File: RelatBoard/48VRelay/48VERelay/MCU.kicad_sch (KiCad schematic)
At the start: 40 parts, among them U1 ESP32-WROOM-32UE, U3 W5500, Y2 ABM3C-25.000MHZ-D4Y-T

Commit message: Update tx / rx nets
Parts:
- R18, R20: footprint Resistor_SMD:R_0603_1608Metric -> Resistor_SMD:R_0201_0603Metric
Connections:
- net PHY_R_RXN: now reaches R16.1, U3.5 (RXN)
- net PHY_RC_RXN: now reaches C17.1, R16.2, R21.1
- net PHY_RC_RXP: now reaches C19.1, R17.2, R22.1
- net PHY_R_TXN: now reaches R7.1, U3.1 (TXN)
- net PHY_R_TXP: now reaches R8.1, U3.2 (TXP)
- net PHY_R_RXP: now reaches R17.1, U3.6 (RXP)
- net TX_N renamed PHY_RC_TXN
- net TX_P renamed PHY_RC_TXP
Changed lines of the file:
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@@
 		)
 	)
+	(label "PHY_R_RXP"
+		(at 210.82 106.68 270)
+		(effects
+			(font
+				(size 1.27 1.27)
+			)
+			(justify right bottom)
+		)
+	)
 	(label "LINK_LED"
 		(at 212.09 129.54 0)
@@
 		)
 	)
+	(label "PHY_RC_TXP"
+		(at 224.79 99.06 90)
+		(effects
+			(font
+				(size 1.27 1.27)
+			)
+			(justify left bottom)
+		)
+	)
 	(label "RX_N"
 		(at 251.46 104.14 0)
@@
 		)
 	)
+	(label "PHY_R_TXP"
+		(at 210.82 99.06 90)
+		(effects
+			(font
+				(size 1.27 1.27)
+			)
+			(justify left bottom)
+		)
+	)
+	(label "PHY_RC_RXN"
+		(at 223.52 104.14 270)
+		(effects
+			(font
+				(size 1.27 1.27)
+			)
+			(justify right bottom)
+		)
+	)
 	(label "Ether_CS"
 		(at 161.29 96.52 0)
@@
 		)
 	)
+	(label "PHY_R_RXN"
+		(at 208.28 104.14 270)
+		(effects
+			(font
+				(size 1.27 1.27)
+			)
+			(justify right bottom)
+		)
+	)
 	(label "PHY_VDD"
 		(at 167.64 83.82 0)
@@
 		)
 	)
+	(label "PHY_R_TXN"
+		(at 208.28 96.52 90)
+		(effects
+			(font
+				(size 1.27 1.27)
+			)
+			(justify left bottom)
+		)
+	)
 	(label "JTAG_TMS"
 		(at 115.57 71.12 0)
@@
 		)
 	)
+	(label "PHY_RC_RXP"
+		(at 224.79 106.68 270)
+		(effects
+			(font
+				(size 1.27 1.27)
+			)
+			(justify right bottom)
+		)
+	)
 	(label "Ether_MOSI"
 		(at 161.29 104.14 0)
@@
 		)
 	)
+	(label "PHY_RC_TXN"
+		(at 222.2454 96.52 90)
+		(effects
+			(font
+				(size 1.27 1.27)
+			)
+			(justify left bottom)
+		)
+	)
 	(label "RX_P"
 		(at 251.46 106.68 0)
@@
 			)
 		)
-		(property "Footprint" "Resistor_SMD:R_0603_1608Metric"
+		(property "Footprint" "Resistor_SMD:R_0201_0603Metric"
 			(at 238.76 90.17 0)
 			(hide yes)
@@
 			)
 		)
-		(property "Footprint" "Resistor_SMD:R_0603_1608Metric"
+		(property "Footprint" "Resistor_SMD:R_0201_0603Metric"
 			(at 228.6 90.17 0)
 			(hide yes)

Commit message: update tx/rx eth routing
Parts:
- R21, R22: footprint Resistor_SMD:R_0201_0603Metric -> Resistor_SMD:R_01005_0402Metric
- R26: footprint (none) -> Resistor_SMD:R_0402_1005Metric
- R6: footprint Resistor_SMD:R_0603_1608Metric -> Resistor_SMD:R_0402_1005Metric
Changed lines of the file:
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@@
 			)
 		)
-		(property "Footprint" "Resistor_SMD:R_0201_0603Metric"
+		(property "Footprint" "Resistor_SMD:R_01005_0402Metric"
 			(at 234.95 111.76 0)
 			(hide yes)
@@
 			)
 		)
-		(property "Footprint" "Resistor_SMD:R_0201_0603Metric"
+		(property "Footprint" "Resistor_SMD:R_01005_0402Metric"
 			(at 228.6 110.49 0)
 			(hide yes)
@@
 			)
 		)
-		(property "Footprint" "Resistor_SMD:R_0603_1608Metric"
+		(property "Footprint" "Resistor_SMD:R_0402_1005Metric"
 			(at 227.33 142.24 0)
 			(hide yes)
@@
 			)
 		)
-		(property "Footprint" ""
+		(property "Footprint" "Resistor_SMD:R_0402_1005Metric"
 			(at 60.452 46.99 90)
 			(hide yes)

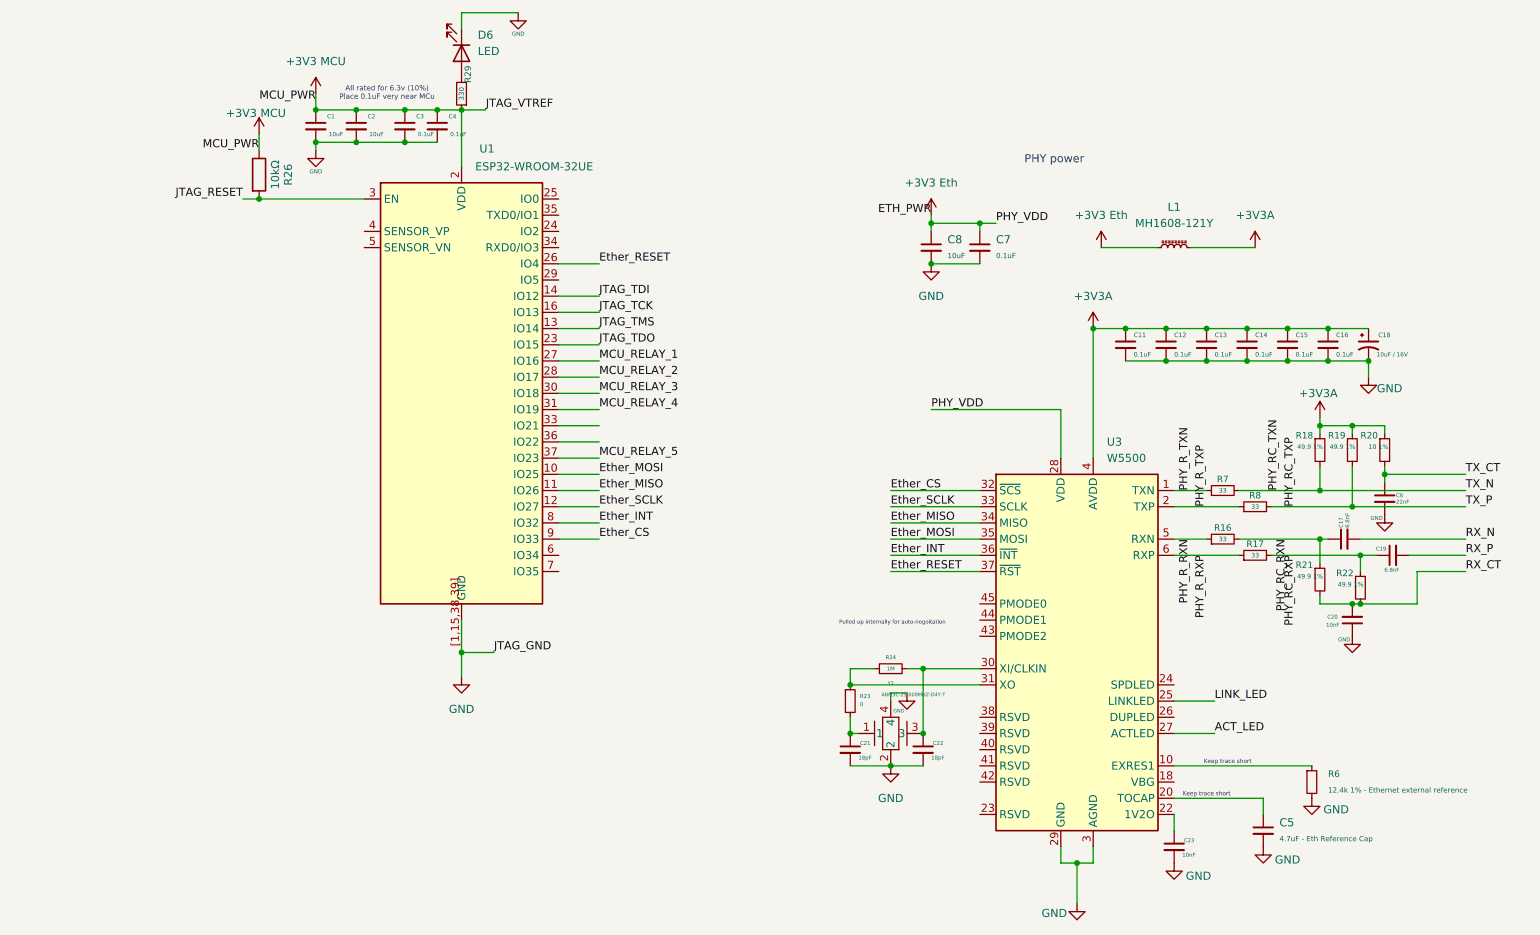
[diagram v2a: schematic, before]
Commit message: JTAG left
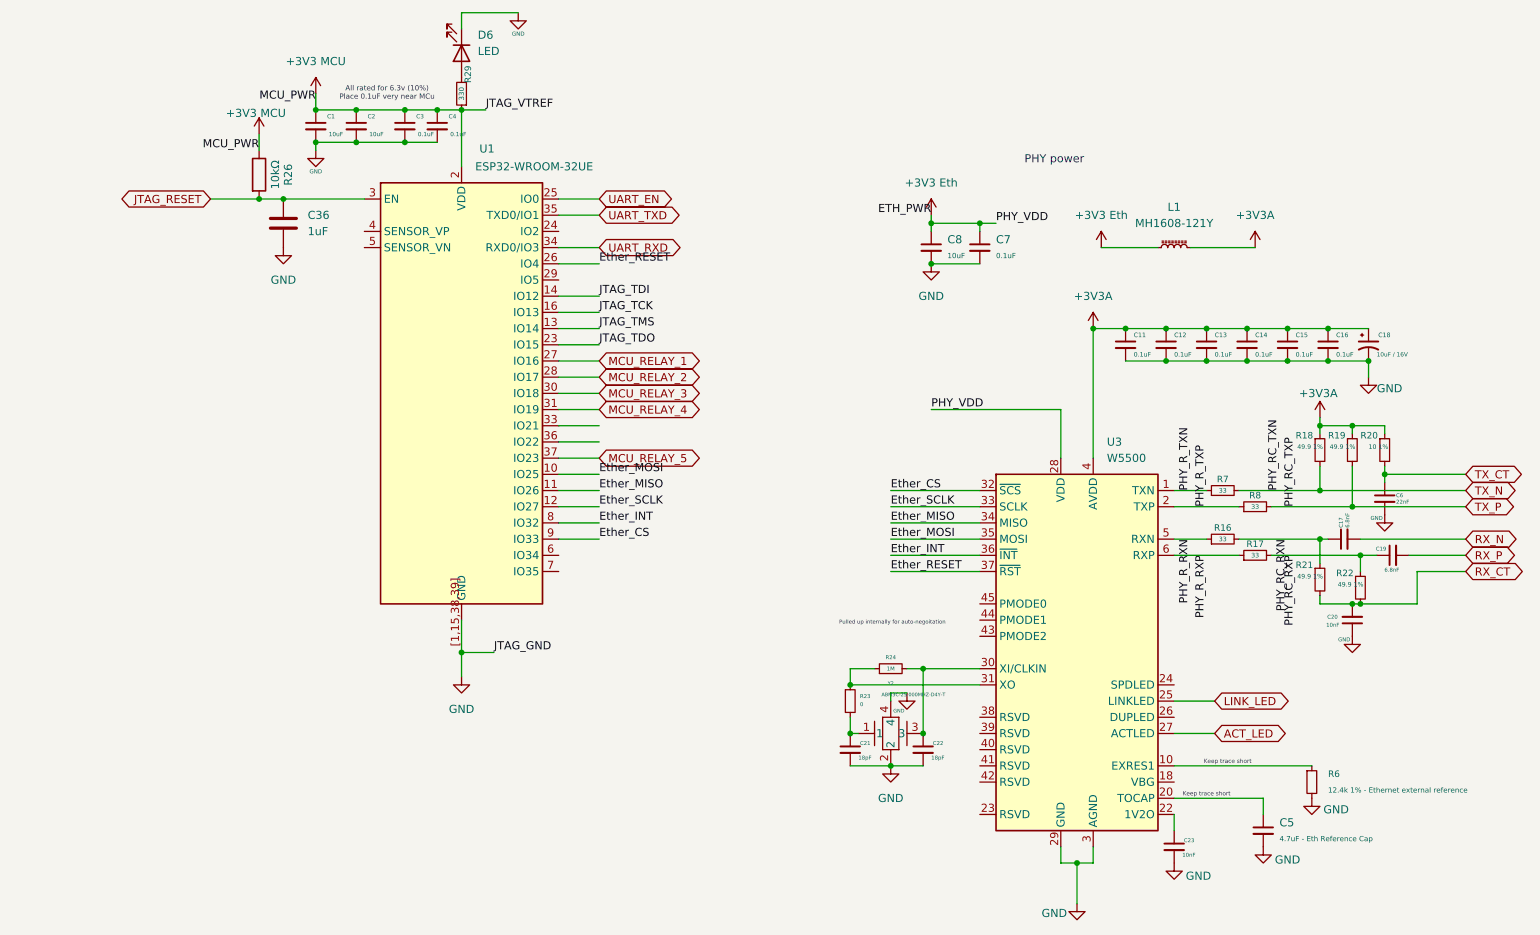
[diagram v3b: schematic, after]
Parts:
- added C36: 1uF, Capacitor_SMD:C_0402_1005Metric, symbol Device:C
- R21, R22: footprint Resistor_SMD:R_01005_0402Metric -> Resistor_SMD:R_0201_0603Metric
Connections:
- net GND: now also C36.2
- net JTAG_RESET: now also C36.1
- net UART_EN: now reaches U1.25 (IO0)
- net UART_RXD: now reaches U1.34 (RXD0/IO3)
- net UART_TXD: now reaches U1.35 (TXD0/IO1)
- net PHY_RC_TXN renamed TX_N
- net PHY_RC_TXP renamed TX_P

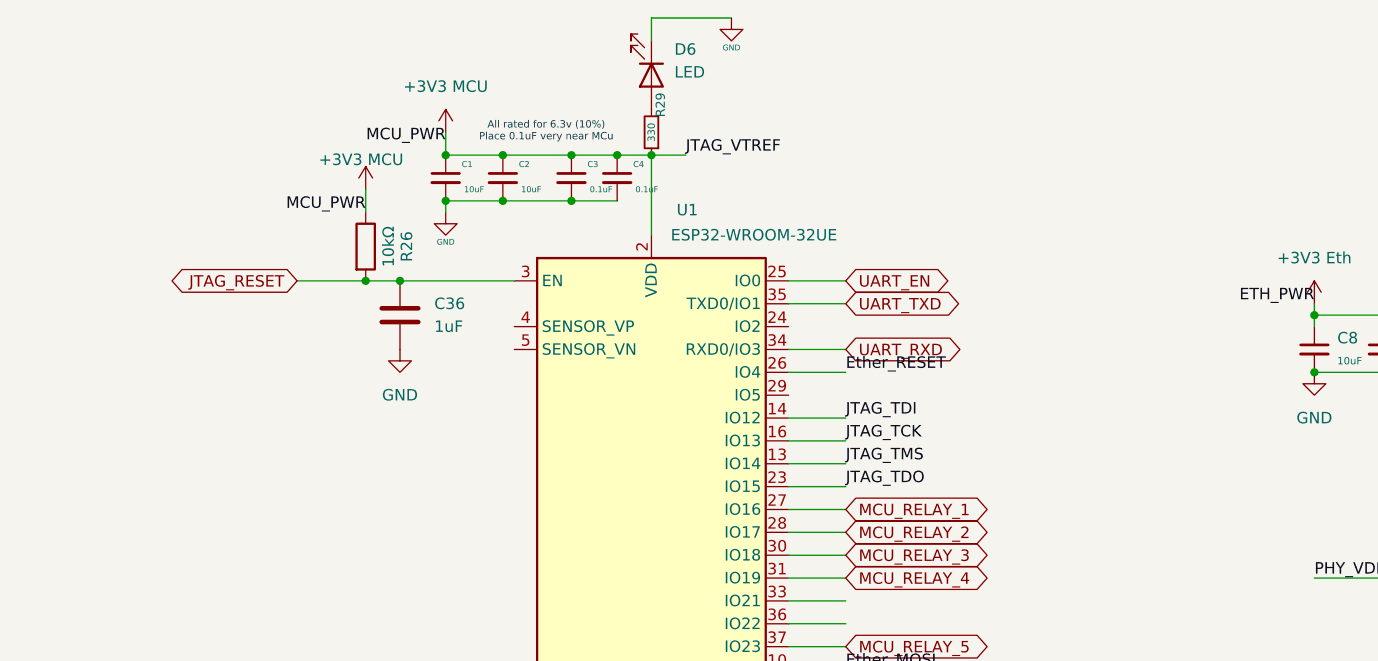
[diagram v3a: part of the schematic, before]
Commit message: update txrx routing length
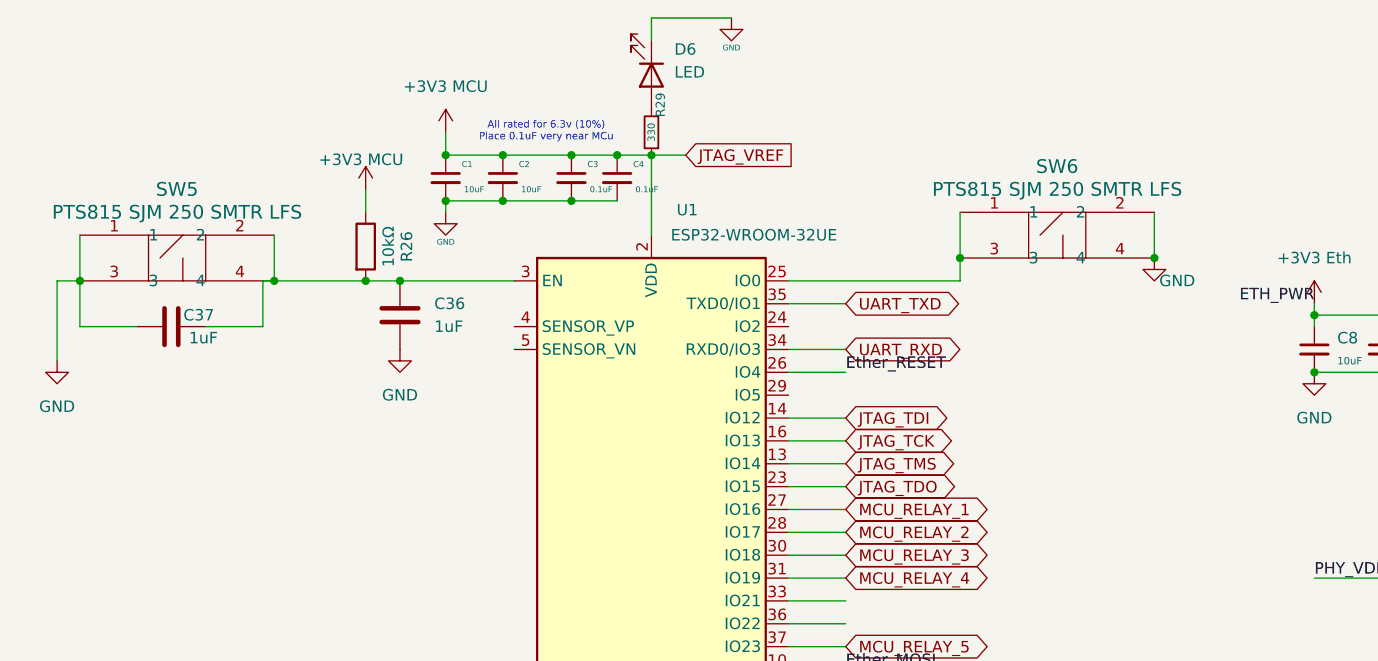
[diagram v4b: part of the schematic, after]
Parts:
- added C37: 1uF, Capacitor_SMD:C_0402_1005Metric, symbol Device:C
- added SW5, SW6: PTS815 SJM 250 SMTR LFS, SW4_PTS815 SJM 250 SMTR LFS_CNK, symbol 2026-07-19_23-07-35:PTS815_SJM_250_SMTR_LFS
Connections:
- net GND: now also C37.2, SW5.1, SW5.3, SW6.2, SW6.4
- net JTAG_RESET: no longer names the net of C36.1, R26.2, U1.3 (EN)
- net JTAG_RESET: now also C37.1, SW5.2, SW5.4
- net UART_EN: no longer names the net of U1.25 (IO0)
- net UART_EN: now also SW6.1, SW6.3

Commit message: wired uart and jtag
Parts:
- SW5: value PTS815 SJM 250 SMTR LFS -> ENABLE; footprint SW4_PTS815 SJM 250 SMTR LFS_CNK -> Button_Switch_THT:SW_PUSH_6mm_H5mm
- SW6: value PTS815 SJM 250 SMTR LFS -> RESET; footprint SW4_PTS815 SJM 250 SMTR LFS_CNK -> Button_Switch_THT:SW_PUSH_6mm_H5mm
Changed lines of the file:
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@@
 	)
 	(junction
-		(at 128.27 48.26)
-		(diameter 0)
-		(color 0 0 0 0)
-	)
-	(junction
 		(at 161.29 139.7)
 		(diameter 0)
@@
 	)
 	(junction
+		(at 128.27 48.26)
+		(diameter 0)
+		(color 0 0 0 0)
+	)
+	(junction
 		(at 154.94 134.62)
 		(diameter 0)
@@
 	(wire
 		(pts
+			(xy 128.27 48.26) (xy 128.27 50.8)
+		)
+		(stroke
+			(width 0)
+			(type default)
+		)
+	)
+	(wire
+		(pts
 			(xy 27.94 59.69) (xy 27.94 50.8)
 		)
@@
 	(wire
 		(pts
-			(xy 128.27 50.8) (xy 128.27 48.26)
-		)
-		(stroke
-			(width 0)
-			(type default)
-		)
-	)
-	(wire
-		(pts
 			(xy 62.23 50.8) (xy 66.04 50.8)
 		)
@@
 	(wire
 		(pts
-			(xy 128.27 43.18) (xy 128.27 48.26)
+			(xy 243.84 109.22) (xy 243.84 114.3)
 		)
 		(stroke
@@
 	(wire
 		(pts
-			(xy 243.84 109.22) (xy 243.84 114.3)
+			(xy 166.37 134.62) (xy 166.37 124.46)
 		)
 		(stroke
@@
 	(wire
 		(pts
-			(xy 166.37 134.62) (xy 166.37 124.46)
+			(xy 228.6 104.14) (xy 215.9 104.14)
 		)
 		(stroke
@@
 	(wire
 		(pts
-			(xy 228.6 104.14) (xy 215.9 104.14)
+			(xy 161.29 104.14) (xy 175.26 104.14)
 		)
 		(stroke
@@
 	(wire
 		(pts
-			(xy 161.29 104.14) (xy 175.26 104.14)
+			(xy 109.22 86.36) (xy 115.57 86.36)
 		)
 		(stroke
@@
 	(wire
 		(pts
-			(xy 109.22 86.36) (xy 115.57 86.36)
+			(xy 154.94 134.62) (xy 154.94 132.08)
 		)
 		(stroke
@@
 	(wire
 		(pts
-			(xy 154.94 134.62) (xy 154.94 132.08)
+			(xy 161.29 101.6) (xy 175.26 101.6)
 		)
 		(stroke
@@
 	(wire
 		(pts
-			(xy 161.29 101.6) (xy 175.26 101.6)
+			(xy 128.27 43.18) (xy 128.27 48.26)
 		)
 		(stroke
@@
 		)
 	)
-	(label "JTAG_GND"
-		(at 99.06 121.92 0)
-		(effects
-			(font
-				(size 1.27 1.27)
-			)
-			(justify left bottom)
-		)
-	)
 	(label "Ether_INT"
 		(at 161.29 106.68 0)
@@
 		)
 	)
+	(global_label "3V3 MCU"
+		(shape input)
+		(at 71.12 34.29 180)
+		(fields_autoplaced yes)
+		(effects
+			(font
+				(size 1.27 1.27)
+			)
+			(justify right)
+		)
+		(property "Intersheetrefs" "${INTERSHEET_REFS}"
+			(at 59.6077 34.29 0)
+			(hide yes)
+			(show_name no)
+			(do_not_autoplace no)
+			(effects
+				(font
+					(size 1.27 1.27)
+				)
+				(justify right)
+			)
+		)
+	)
 	(global_label "UART_RXD"
 		(shape bidirectional)
@@
 		)
 	)
+	(global_label "GND"
+		(shape bidirectional)
+		(at 99.06 121.92 0)
+		(fields_autoplaced yes)
+		(effects
+			(font
+				(size 1.27 1.27)
+			)
+			(justify left)
+		)
+		(property "Intersheetrefs" "${INTERSHEET_REFS}"
+			(at 107.027 121.92 0)
+			(hide yes)
+			(show_name no)
+			(do_not_autoplace no)
+			(effects
+				(font
+					(size 1.27 1.27)
+				)
+				(justify left)
+			)
+		)
+	)
 	(global_label "MCU_RELAY_1"
 		(shape bidirectional)
@@
 			)
 		)
-		(property "Value" "PTS815 SJM 250 SMTR LFS"
+		(property "Value" "ENABLE"
 			(at 41.275 43.18 0)
 			(show_name no)
@@
 			)
 		)
-		(property "Footprint" "SW4_PTS815 SJM 250 SMTR LFS_CNK"
+		(property "Footprint" "Button_Switch_THT:SW_PUSH_6mm_H5mm"
 			(at 38.1 55.88 0)
 			(hide yes)
@@
 			)
 		)
-		(property "Value" "PTS815 SJM 250 SMTR LFS"
+		(property "Value" "RESET"
 			(at 139.065 40.64 0)
 			(show_name no)
@@
 			)
 		)
-		(property "Footprint" "SW4_PTS815 SJM 250 SMTR LFS_CNK"
+		(property "Footprint" "Button_Switch_THT:SW_PUSH_6mm_H5mm"
 			(at 135.89 53.34 0)
 			(hide yes)

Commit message: Final design
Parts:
- D6: footprint LED_SMD:LED_0201_0603Metric -> LED_SMD:LED_0603_1608Metric
- Y2: footprint Library:CRYSTAL_ABM3C_ABR-M -> Crystal:Crystal_SMD_Abracon_ABM3C-4Pin_5.0x3.2mm
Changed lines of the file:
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@@
 			)
 		)
-		(property "Footprint" "LED_SMD:LED_0201_0603Metric"
+		(property "Footprint" "LED_SMD:LED_0603_1608Metric"
 			(at 93.98 27.94 0)
 			(hide yes)
@@
 		(dnp no)
 		(property "Reference" "Y2"
-			(at 161.29 126.746 0)
+			(at 157.988 131.318 0)
 			(show_name no)
 			(do_not_autoplace no)
@@
 			)
 		)
-		(property "Footprint" "Library:CRYSTAL_ABM3C_ABR-M"
+		(property "Footprint" "Crystal:Crystal_SMD_Abracon_ABM3C-4Pin_5.0x3.2mm"
 			(at 156.21 134.62 0)
 			(hide yes)
